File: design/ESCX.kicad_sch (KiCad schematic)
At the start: 18 parts, among them J1 HALL_ENC, J4 SWD, J5 USB_OTG, SW1 SENSOR_VOLTAGE

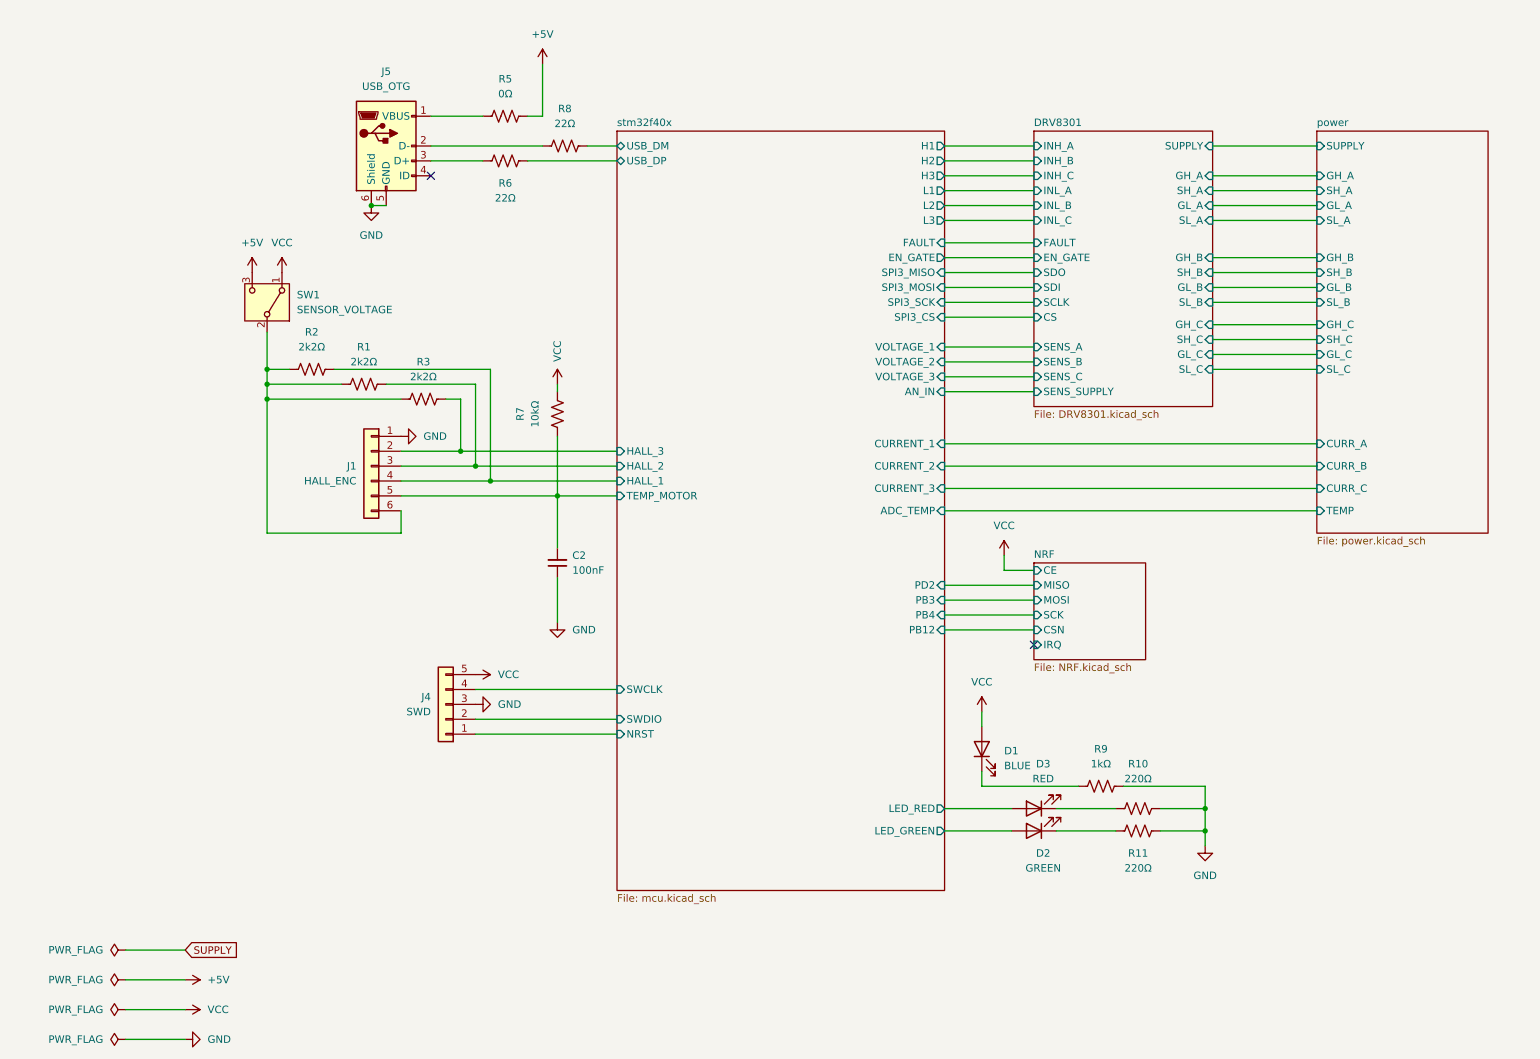
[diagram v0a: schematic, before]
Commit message: Cambie a USB C
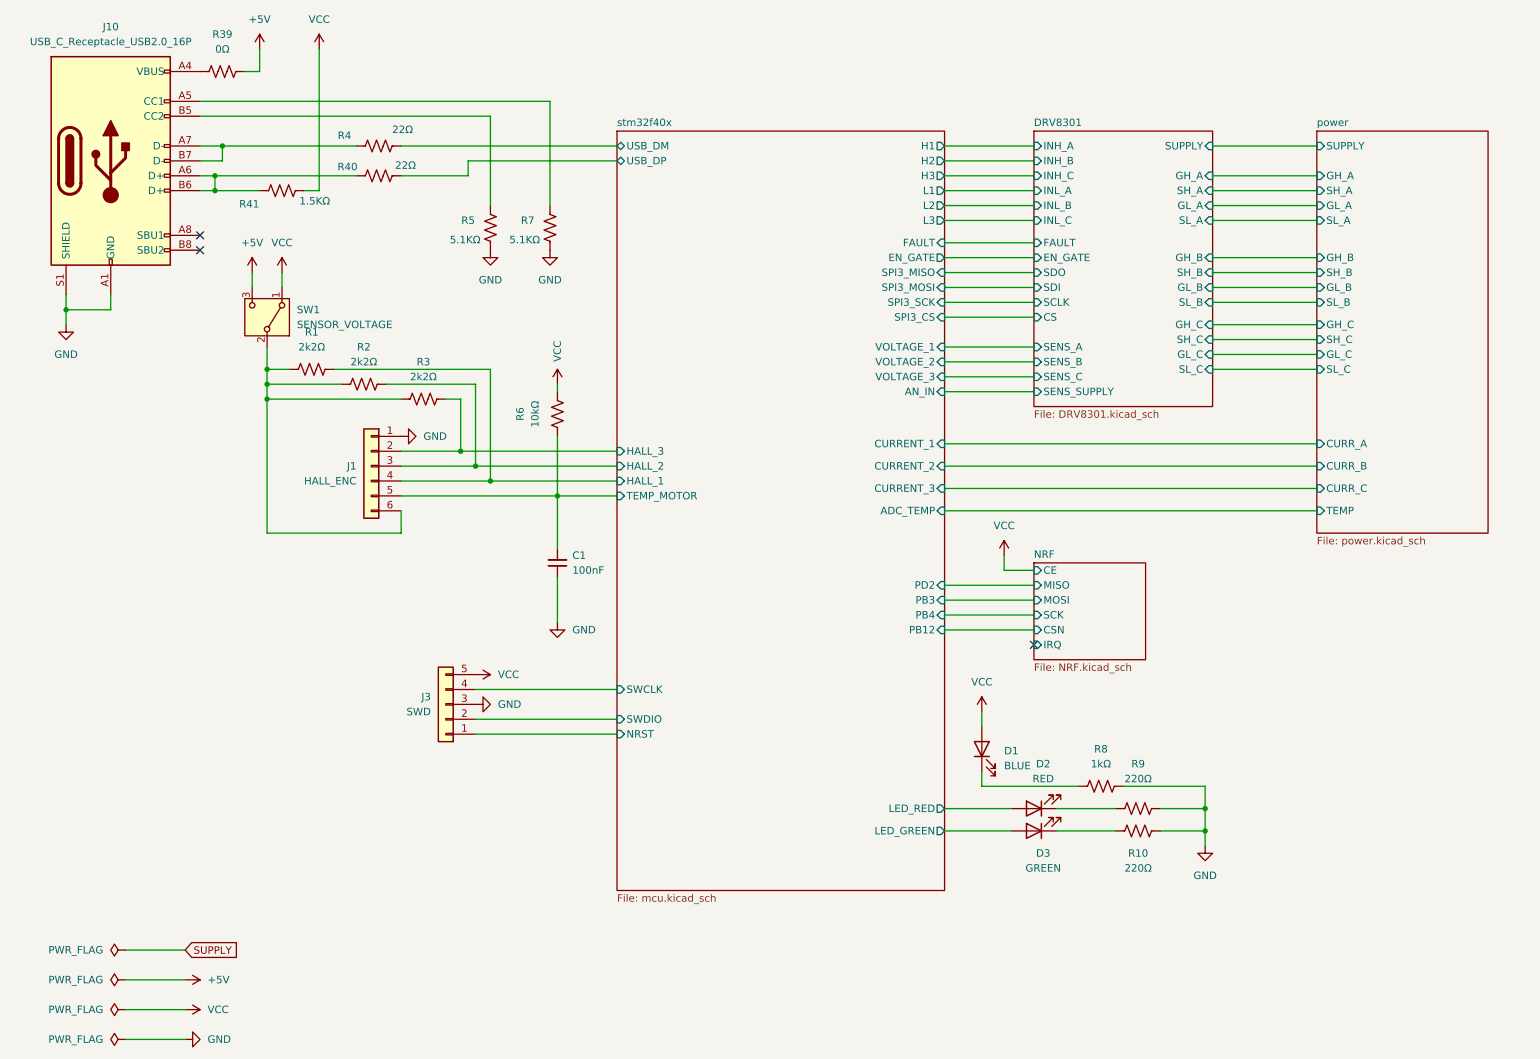
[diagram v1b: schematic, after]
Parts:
- removed J5: USB_OTG, symbol bldc:USB_OTG
- removed R6, R8: 22Ω, Resistor_SMD:R_0603_1608Metric, symbol Device:R_US
- added J10: USB_C_Receptacle_USB2.0_16P, symbol Connector:USB_C_Receptacle_USB2.0_16P
- added R39: 0Ω, Resistor_SMD:R_0603_1608Metric, symbol Device:R_US
- added R4, R40: 22Ω, Resistor_SMD:R_0603_1608Metric, symbol Device:R_US
- added R41: 1.5KΩ, Resistor_SMD:R_0603_1608Metric, symbol Device:R_US
- added R7: 5.1KΩ, Resistor_SMD:R_0603_1608Metric, symbol Device:R_US
- J1: Manufacturer (none) -> JST; Manufacturer Product Number  (none) -> B6B-XH-A
- J3: renamed from J4; Manufacturer (none) -> JST; Manufacturer Product Number  (none) -> B5B-XH-A
- R5: value 0Ω -> 5.1KΩ; Manufacturer Product Number  RC0603JR-070RL -> RC0603FR-0722RL
- renumbered C2 to C1, D3 to D2, D2 to D3, R2 to R1, R11 to R10, R1 to R2, R7 to R6, R9 to R8, R10 to R9
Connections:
- net +5V: now also R39.1; no longer R5.1
- net GND: now also R5.1, J10.A1 (GND), J10.A12 (GND), J10.B1 (GND), J10.B12 (GND), J10.S1 (SHIELD), R7.1
- net VCC: now also R41.1
- net stm32f40x/USB_DM: now also R4.1
- net stm32f40x/USB_DP: now also R40.1
- net at R5.2: now also J10.B5 (CC2)
- new net: J10.A4 (VBUS), J10.A9 (VBUS), J10.B4 (VBUS), J10.B9 (VBUS), R39.2
- new net: J10.A7 (D-), J10.B7 (D-), R4.2
- new net: J10.A5 (CC1), R7.2
- new net: J10.A6 (D+), J10.B6 (D+), R40.2, R41.2
- no-connect marks 2 -> 3
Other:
- moved on the sheet: SW1

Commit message: Agregue Manufacturer Product Number
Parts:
- J1: renamed from J10; footprint (none) -> Connector_USB:USB_C_Receptacle_GCT_USB4105-xx-A_16P_TopMnt_Horizontal
- J2: renamed from J1; footprint (none) -> Connector_JST:JST_XH_B6B-XH-AM_1x06_P2.50mm_Vertical
- J3: footprint (none) -> Connector_JST:JST_XH_B5B-XH-AM_1x05_P2.50mm_Vertical
- R2: renamed from R41; Manufacturer Product Number  RC0603FR-0722RL -> RC0603FR-071K5L
- R8: renamed from R5; Manufacturer Product Number  RC0603FR-0722RL -> RC0603FR-075K1L
- R9: renamed from R7; Manufacturer Product Number  RC0603FR-0722RL -> RC0603FR-075K1L
- renumbered R39 to R1, R6 to R10, R8 to R11, R9 to R12, R10 to R13, R1 to R3, R2 to R4, R4 to R5, R40 to R6, R3 to R7

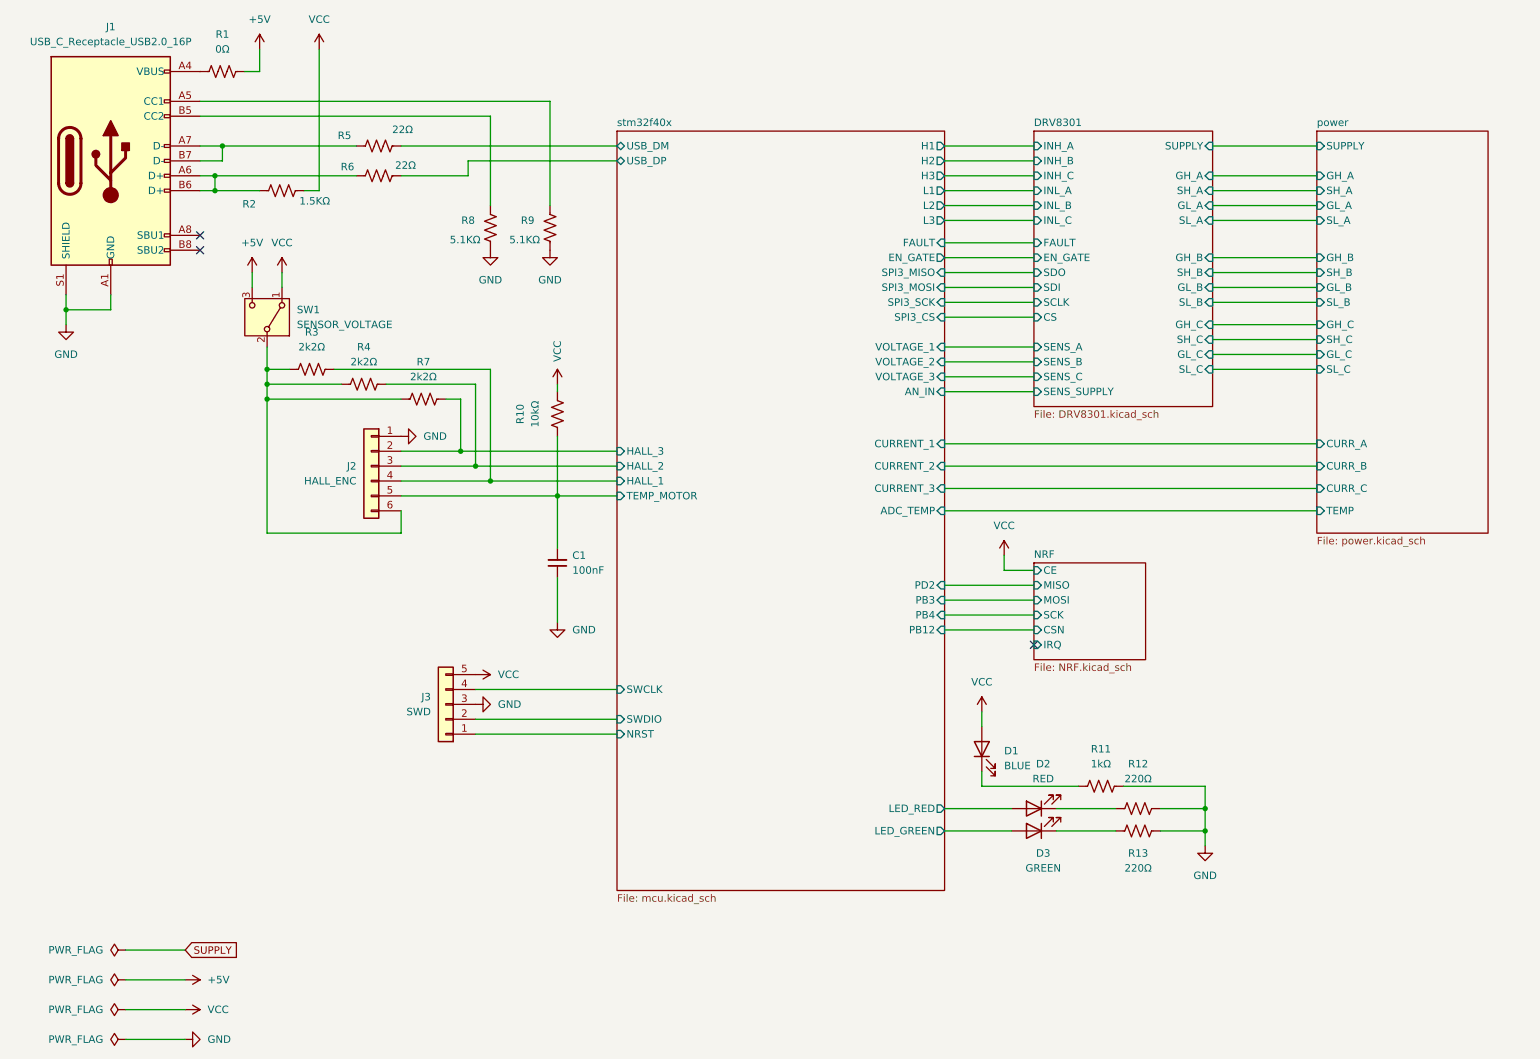
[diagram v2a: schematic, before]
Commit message: Ordenado del esquemático
- Cambios en los capacitores del oscilador
- Mejora de los esquemáticos, encapsulado la interfáz usb y los sensores del motor
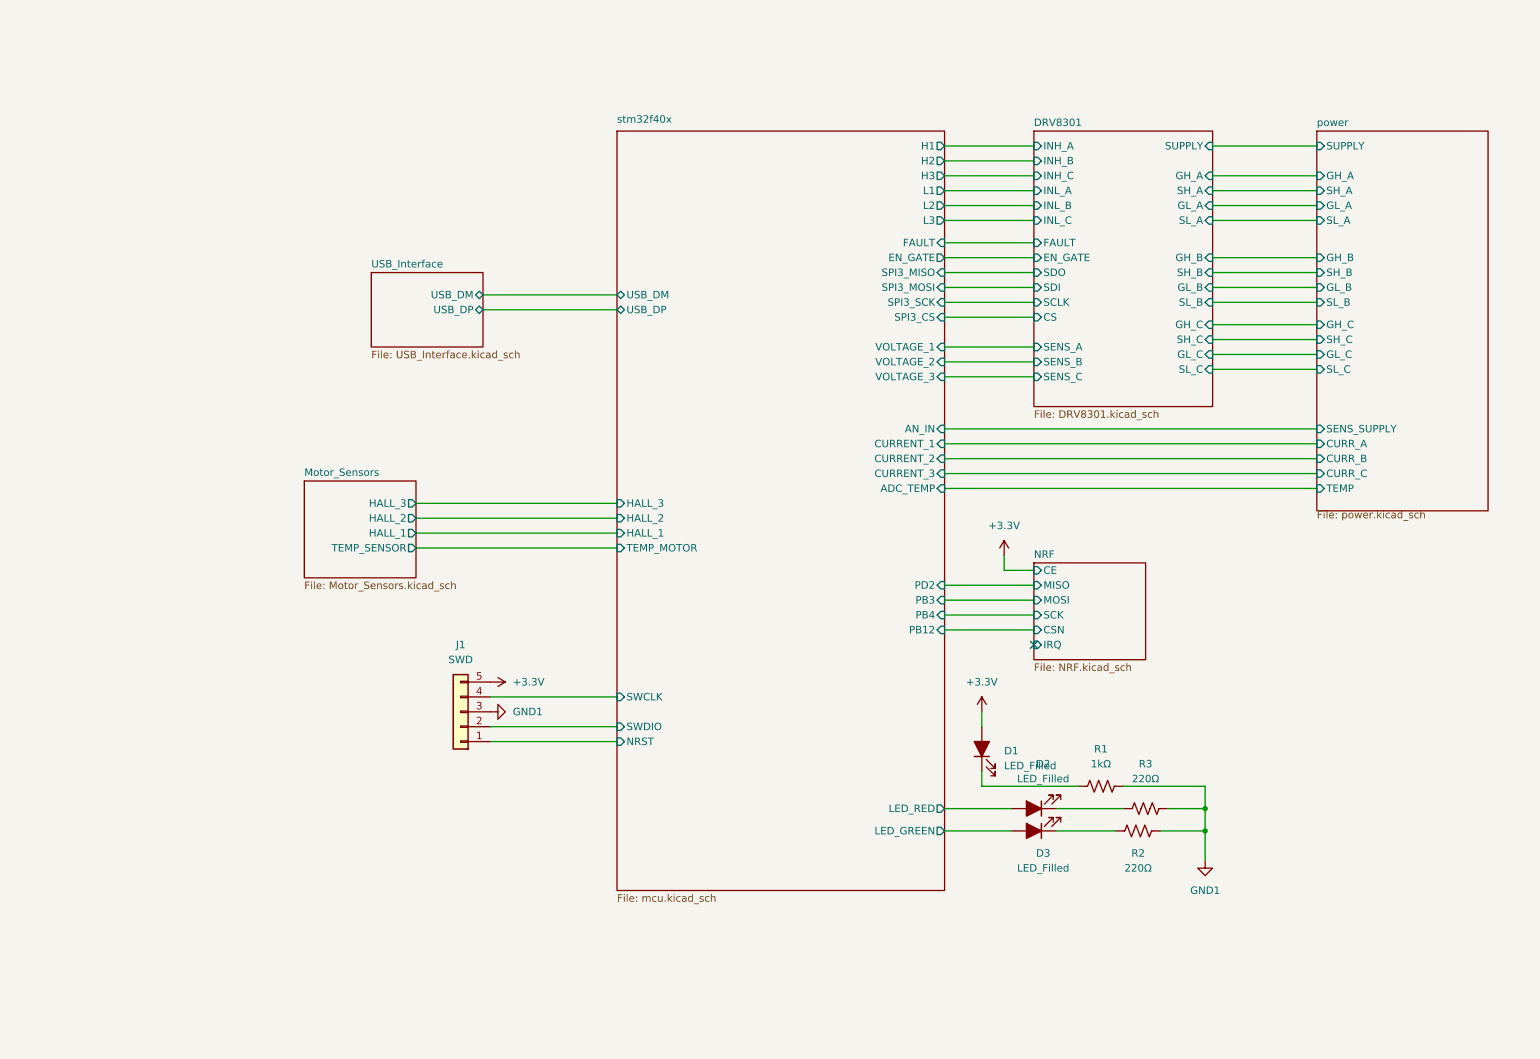
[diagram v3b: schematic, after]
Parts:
- removed C1: 100nF, Capacitor_SMD:C_0603_1608Metric, symbol Device:C_Small
- removed J1: USB_C_Receptacle_USB2.0_16P, Connector_USB:USB_C_Receptacle_GCT_USB4105-xx-A_16P_TopMnt_Horizontal, symbol Connector:USB_C_Receptacle_USB2.0_16P
- removed J2: HALL_ENC, Connector_JST:JST_XH_B6B-XH-AM_1x06_P2.50mm_Vertical, symbol Connector_Generic:Conn_01x06
- removed R1: 0Ω, Resistor_SMD:R_0603_1608Metric, symbol Device:R_US
- removed R10: 10kΩ, Resistor_SMD:R_0603_1608Metric, symbol Device:R_US
- removed R2: 1.5KΩ, Resistor_SMD:R_0603_1608Metric, symbol Device:R_US
- removed R3, R4, R7: 2k2Ω, Resistor_SMD:R_0603_1608Metric, symbol Device:R_US
- removed R5, R6: 22Ω, Resistor_SMD:R_0603_1608Metric, symbol Device:R_US
- removed R8, R9: 5.1KΩ, Resistor_SMD:R_0603_1608Metric, symbol Device:R_US
- removed SW1: SENSOR_VOLTAGE, Button_Switch_THT:SW_Slide-03_Wuerth-WS-SLTV_10x2.5x6.4_P2.54mm, symbol Switch:SW_SPDT
- D1: value BLUE -> LED_Filled; symbol Device:LED -> Device:LED_Filled
- D2: value RED -> LED_Filled; symbol Device:LED -> Device:LED_Filled
- D3: value GREEN -> LED_Filled; symbol Device:LED -> Device:LED_Filled
- renumbered J3 to J1, R11 to R1, R13 to R2, R12 to R3
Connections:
- net GND renamed GND1
- net VCC renamed +3.3V
- no-connect marks 3 -> 1
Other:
- added sheet Motor_Sensors (Motor_Sensors.kicad_sch)
- added sheet USB_Interface (USB_Interface.kicad_sch)
- sheet DRV8301 ports: added none; removed SENS_SUPPLY
- sheet power ports: added SENS_SUPPLY; removed none
- moved on the sheet: J1, R3

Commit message: Pequeños cambios
Pequeños cambios, eliminado de carpeta BLDC
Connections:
- net GND1: now also R1.1; no longer R1.2
- net at D1.1 (K): now also R1.2; no longer R1.1
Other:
- sheet stm32f40x renamed MCU
- sheet MCU: file mcu.kicad_sch -> MCU.kicad_sch
- moved on the sheet: R3

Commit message: Pequeños cambios
Pequeños cambios en esquemático
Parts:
- renumbered D2 to D1, D3 to D2, D1 to D3, R3 to R1, R1 to R3
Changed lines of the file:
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@@
 		(dnp no)
 		(fields_autoplaced yes)
-		(property "Reference" "D2"
+		(property "Reference" "D1"
 			(at 189.5475 140.97 0)
 			(effects
@@
 			(project "ESCX"
 				(path "/6389d757-a1bd-4c0a-9d55-6114b19cc67a"
-					(reference "D2")
+					(reference "D1")
 					(unit 1)
 				)
@@
 		(dnp no)
 		(fields_autoplaced yes)
-		(property "Reference" "D3"
+		(property "Reference" "D2"
 			(at 189.5475 156.21 0)
 			(effects
@@
 			(project "ESCX"
 				(path "/6389d757-a1bd-4c0a-9d55-6114b19cc67a"
-					(reference "D3")
+					(reference "D2")
 					(unit 1)
 				)
@@
 		(dnp no)
 		(fields_autoplaced yes)
-		(property "Reference" "R3"
+		(property "Reference" "R1"
 			(at 205.74 142.24 90)
 			(effects
@@
 			(project "ESCX"
 				(path "/6389d757-a1bd-4c0a-9d55-6114b19cc67a"
-					(reference "R3")
+					(reference "R1")
 					(unit 1)
 				)
@@
 		(dnp no)
 		(fields_autoplaced yes)
-		(property "Reference" "#PWR03"
+		(property "Reference" "#PWR04"
 			(at 217.17 129.54 0)
 			(effects
@@
 			(project "ESCX"
 				(path "/6389d757-a1bd-4c0a-9d55-6114b19cc67a"
-					(reference "#PWR03")
+					(reference "#PWR04")
 					(unit 1)
 				)
@@
 		(dnp no)
 		(fields_autoplaced yes)
-		(property "Reference" "#PWR04"
+		(property "Reference" "#PWR03"
 			(at 182.88 109.22 0)
 			(effects
@@
 			(project "ESCX"
 				(path "/6389d757-a1bd-4c0a-9d55-6114b19cc67a"
-					(reference "#PWR04")
+					(reference "#PWR03")
 					(unit 1)
 				)
@@
 		(dnp no)
 		(fields_autoplaced yes)
-		(property "Reference" "D1"
+		(property "Reference" "D3"
 			(at 220.98 132.3974 90)
 			(effects
@@
 			(project "ESCX"
 				(path "/6389d757-a1bd-4c0a-9d55-6114b19cc67a"
-					(reference "D1")
+					(reference "D3")
 					(unit 1)
 				)
@@
 		(dnp no)
 		(fields_autoplaced yes)
-		(property "Reference" "R1"
+		(property "Reference" "R3"
 			(at 219.71 140.9699 0)
 			(effects
@@
 			(project "ESCX"
 				(path "/6389d757-a1bd-4c0a-9d55-6114b19cc67a"
-					(reference "R1")
+					(reference "R3")
 					(unit 1)
 				)

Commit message: Agrego MFR# de conectores
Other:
- moved on the sheet: D1, D2, D3, J1, R1, R2, R3
